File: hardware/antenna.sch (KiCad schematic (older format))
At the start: 9 parts, among them P1 SATA

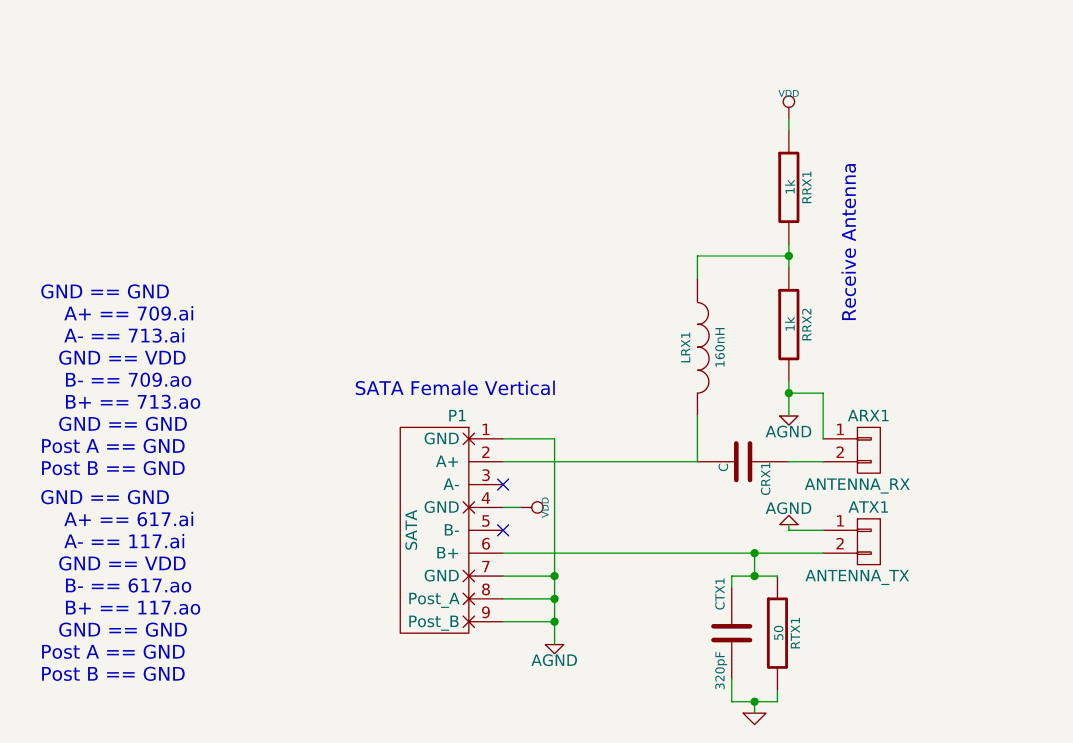
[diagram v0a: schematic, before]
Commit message: Initial PCB layout for antenna
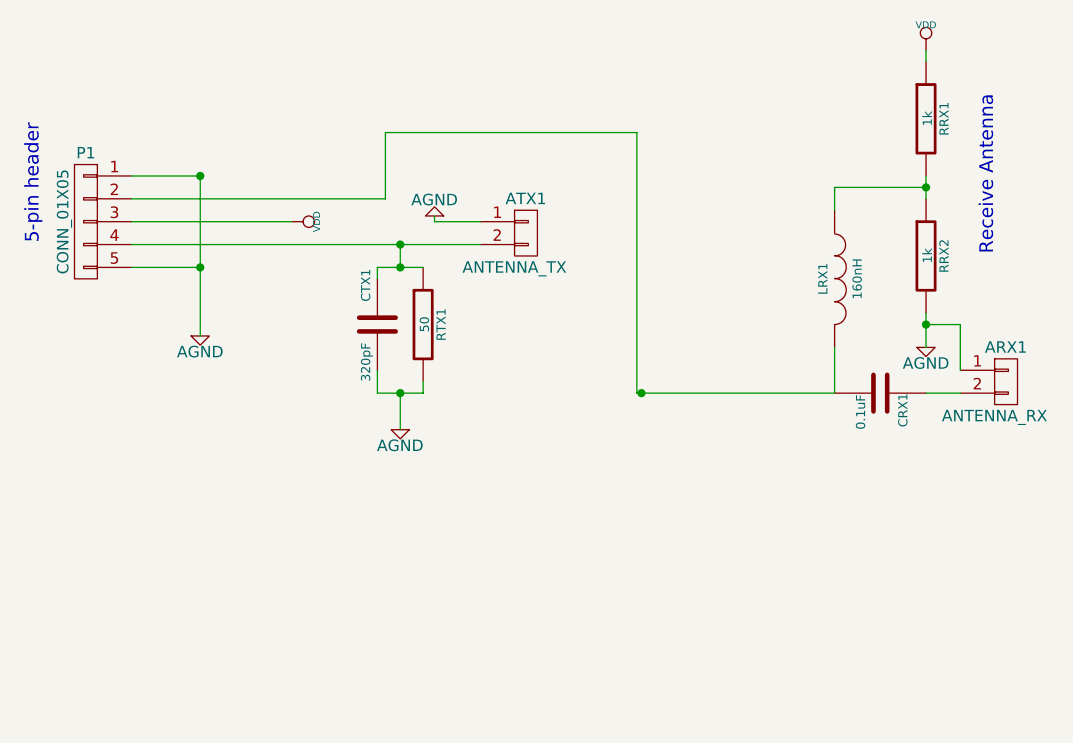
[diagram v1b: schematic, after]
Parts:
- removed P1: SATA, symbol SATA
- added P1: CONN_01X05, Pin_Headers:Pin_Header_Straight_1x05, symbol CONN_01X05
- CRX1: value C -> 0.1uF
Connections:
- net labels removed: GND
- wire segments 26 -> 29
- no-connect marks 2 -> 0
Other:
- note added: "5-pin header"
- note removed: "GND == GND\n A+ == 617.ai\n A- == 117.ai\n GND == VDD\n B- == 617.ao\n B+ == 117.ao\n GND == GND\nPost A == GND\nPost B == GND"
- note removed: "GND == GND\n A+ == 709.ai\n A- == 713.ai\n GND == VDD\n B- == 709.ao\n B+ == 713.ao\n GND == GND\nPost A == GND\nPost B == GND"
- note removed: "SATA Female Vertical"
- moved on the sheet: ARX1, ATX1, CRX1, CTX1, LRX1, RRX1, RRX2, RTX1

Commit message: Fixing up the antenna board.
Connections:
- wire segments 29 -> 28
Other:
- note added: "Transmitt Antenna"
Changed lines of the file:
@@
 LIBS:sata
 LIBS:antenna-cache
-EELAYER 24 0
+EELAYER 25 0
 EELAYER END
 $Descr User 5827 4134
@@
 $EndComp
 Wire Wire Line
-	2825 1450 1300 1450
+	1300 1450 2825 1450
 Wire Wire Line
 	2000 1350 1300 1350
@@
 Connection ~ 4775 1800
 Wire Wire Line
-	3525 2100 4375 2100
-Wire Wire Line
 	1300 1550 1600 1550
 Connection ~ 1600 1550
@@
 	3510 960  3510 2100
 Wire Wire Line
-	3510 2100 3530 2100
-Connection ~ 3530 2100
+	3510 2100 4375 2100
+Text Notes 2185 1485 3    60   ~ 0
+Transmitt Antenna
 $EndSCHEMATC
